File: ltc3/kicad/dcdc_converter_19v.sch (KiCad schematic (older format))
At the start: 4 parts

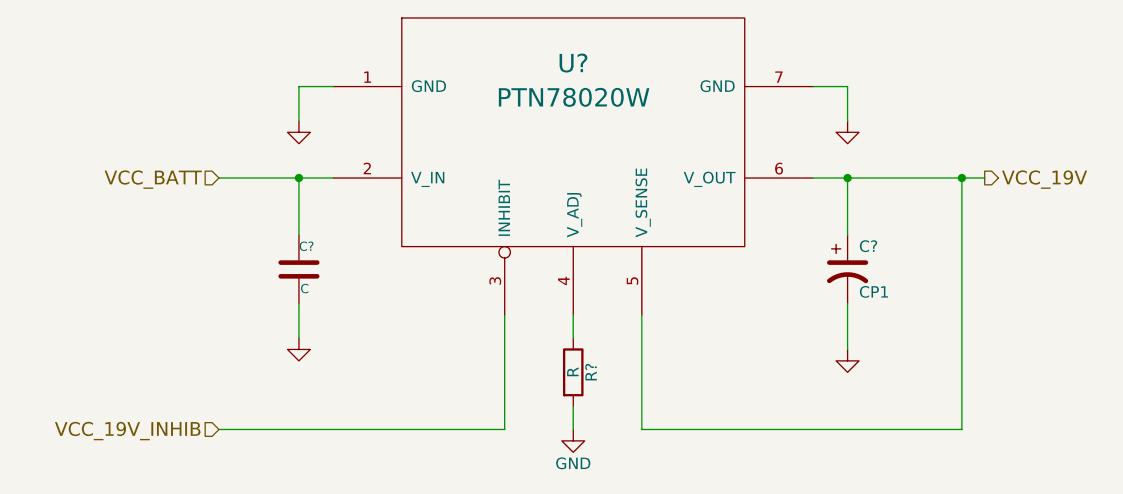
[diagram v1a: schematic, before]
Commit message: Fixed annoying obsolete library component warning (again). Had to delete the -cache.lib file.
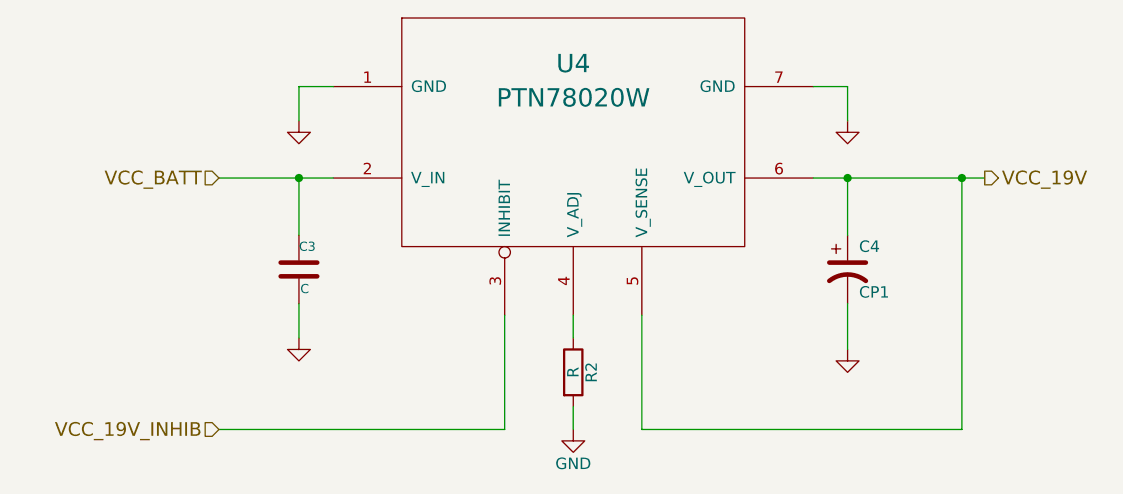
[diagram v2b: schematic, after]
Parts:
- gave numbers to parts that had none: 4
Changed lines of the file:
@@
 LIBS:memory
 LIBS:xilinx
-LIBS:special
 LIBS:microcontrollers
 LIBS:dsp
@@
 LIBS:contrib
 LIBS:valves
+LIBS:headers
+LIBS:DIP_switches
+LIBS:LTC299x
+LIBS:memory_devices
+LIBS:switches
+LIBS:Toshiba
 LIBS:LTC3_components
 LIBS:Launch_Tower_Computer_III-cache
-EELAYER 27 0
+EELAYER 25 0
 EELAYER END
 $Descr B 17000 11000
@@
 VCC_BATT
 $Comp
-L PTN78020W U?
+L PTN78020W U4
 U 1 1 555D15B9
 P 8350 4550
-F 0 "U?" H 8350 4850 80  0000 C CNN
+F 0 "U4" H 8350 4850 80  0000 C CNN
 F 1 "PTN78020W" H 8350 4700 80  0000 C CNN
 F 2 "~" H 8350 4600 60  0000 C CNN
@@
 $EndComp
 $Comp
-L GND #PWR?
+L GND #PWR6
 U 1 1 555D15C0
 P 7150 4500
-F 0 "#PWR?" H 7150 4500 30  0001 C CNN
+F 0 "#PWR6" H 7150 4500 30  0001 C CNN
 F 1 "GND" H 7150 4430 30  0001 C CNN
 F 2 "" H 7150 4500 60  0000 C CNN
@@
 $EndComp
 $Comp
-L GND #PWR?
+L GND #PWR9
 U 1 1 555D15C6
 P 9550 4500
-F 0 "#PWR?" H 9550 4500 30  0001 C CNN
+F 0 "#PWR9" H 9550 4500 30  0001 C CNN
 F 1 "GND" H 9550 4430 30  0001 C CNN
 F 2 "" H 9550 4500 60  0000 C CNN
@@
 	6800 4750 7300 4750
 $Comp
-L CP1 C?
+L CP1 C4
 U 1 1 555D15D2
 P 9550 5150
-F 0 "C?" H 9600 5250 50  0000 L CNN
+F 0 "C4" H 9600 5250 50  0000 L CNN
 F 1 "CP1" H 9600 5050 50  0000 L CNN
 F 2 "~" H 9550 5150 60  0000 C CNN
@@
 $EndComp
 $Comp
-L GND #PWR?
+L GND #PWR10
 U 1 1 555D15D9
 P 9550 5500
-F 0 "#PWR?" H 9550 5500 30  0001 C CNN
+F 0 "#PWR10" H 9550 5500 30  0001 C CNN
 F 1 "GND" H 9550 5430 30  0001 C CNN
 F 2 "" H 9550 5500 60  0000 C CNN
@@
 	9550 5300 9550 5500
 $Comp
-L C C?
+L C C3
 U 1 1 555D15E2
 P 7150 5150
-F 0 "C?" H 7150 5250 40  0000 L CNN
+F 0 "C3" H 7150 5250 40  0000 L CNN
 F 1 "C" H 7156 5065 40  0000 L CNN
 F 2 "~" H 7188 5000 30  0000 C CNN
@@
 $EndComp
 $Comp
-L GND #PWR?
+L GND #PWR7
 U 1 1 555D15E9
 P 7150 5450
-F 0 "#PWR?" H 7150 5450 30  0001 C CNN
+F 0 "#PWR7" H 7150 5450 30  0001 C CNN
 F 1 "GND" H 7150 5380 30  0001 C CNN
 F 2 "" H 7150 5450 60  0000 C CNN
@@
 Connection ~ 7150 4750
 $Comp
-L R R?
+L R R2
 U 1 1 555D15F2
 P 8350 5600
-F 0 "R?" V 8430 5600 50  0000 C CNN
+F 0 "R2" V 8430 5600 50  0000 C CNN
 F 1 "R" V 8350 5600 50  0000 C CNN
 F 2 "" V 8280 5600 30  0000 C CNN
@@
 $EndComp
 $Comp
-L GND #PWR?
+L GND #PWR8
 U 1 1 555D15F9
 P 8350 5850
-F 0 "#PWR?" H 8350 5600 50  0001 C CNN
+F 0 "#PWR8" H 8350 5600 50  0001 C CNN
 F 1 "GND" H 8350 5700 50  0000 C CNN
 F 2 "" H 8350 5850 60  0000 C CNN
